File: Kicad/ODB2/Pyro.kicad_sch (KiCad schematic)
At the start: 33 parts, among them U11 TLV2372, U12 74LVC2G08GT_115, U13 TLV2372

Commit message: ajout footprints
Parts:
- Pyros_LED1, Pyros_LED2, Pyros_LED3: footprint (none) -> LED_SMD:LED_0805_2012Metric
- Pyros_R1, Pyros_R10, Pyros_R11, Pyros_R12, Pyros_R13, Pyros_R14, Pyros_R15, Pyros_R16, Pyros_R17, Pyros_R18, Pyros_R19, Pyros_R2, Pyros_R3, Pyros_R4, Pyros_R5, Pyros_R6, Pyros_R7, Pyros_R8, Pyros_R9: footprint (none) -> Resistor_SMD:R_0805_2012Metric
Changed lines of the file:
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@@
 			)
 		)
-		(property "Footprint" ""
+		(property "Footprint" "Resistor_SMD:R_0805_2012Metric"
 			(at 166.37 36.322 90)
 			(effects
@@
 			)
 		)
-		(property "Footprint" ""
+		(property "Footprint" "LED_SMD:LED_0805_2012Metric"
 			(at 95.25 176.53 0)
 			(effects
@@
 			)
 		)
-		(property "Footprint" ""
+		(property "Footprint" "Resistor_SMD:R_0805_2012Metric"
 			(at 151.13 97.282 90)
 			(effects
@@
 			)
 		)
-		(property "Footprint" ""
+		(property "Footprint" "Resistor_SMD:R_0805_2012Metric"
 			(at 41.91 96.012 90)
 			(effects
@@
 			)
 		)
-		(property "Footprint" ""
+		(property "Footprint" "Resistor_SMD:R_0805_2012Metric"
 			(at 56.388 72.39 90)
 			(effects
@@
 			)
 		)
-		(property "Footprint" ""
+		(property "Footprint" "Resistor_SMD:R_0805_2012Metric"
 			(at 71.882 82.55 90)
 			(effects
@@
 			)
 		)
-		(property "Footprint" ""
+		(property "Footprint" "Resistor_SMD:R_0805_2012Metric"
 			(at 173.228 43.18 90)
 			(effects
@@
 			)
 		)
-		(property "Footprint" ""
+		(property "Footprint" "Resistor_SMD:R_0805_2012Metric"
 			(at 50.038 104.14 90)
 			(effects
@@
 			)
 		)
-		(property "Footprint" ""
+		(property "Footprint" "Resistor_SMD:R_0805_2012Metric"
 			(at 181.102 83.82 90)
 			(effects
@@
 			)
 		)
-		(property "Footprint" ""
+		(property "Footprint" "Resistor_SMD:R_0805_2012Metric"
 			(at 168.148 109.22 90)
 			(effects
@@
 			)
 		)
-		(property "Footprint" ""
+		(property "Footprint" "Resistor_SMD:R_0805_2012Metric"
 			(at 58.928 107.95 90)
 			(effects
@@
 			)
 		)
-		(property "Footprint" ""
+		(property "Footprint" "Resistor_SMD:R_0805_2012Metric"
 			(at 165.608 73.66 90)
 			(effects
@@
 			)
 		)
-		(property "Footprint" ""
+		(property "Footprint" "Resistor_SMD:R_0805_2012Metric"
 			(at 57.15 35.052 90)
 			(effects
@@
 			)
 		)
-		(property "Footprint" ""
+		(property "Footprint" "Resistor_SMD:R_0805_2012Metric"
 			(at 41.91 174.752 90)
 			(effects
@@
 			)
 		)
-		(property "Footprint" ""
+		(property "Footprint" "LED_SMD:LED_0805_2012Metric"
 			(at 52.07 176.53 0)
 			(effects
@@
 			)
 		)
-		(property "Footprint" ""
+		(property "Footprint" "Resistor_SMD:R_0805_2012Metric"
 			(at 78.74 57.658 90)
 			(effects
@@
 			)
 		)
-		(property "Footprint" ""
+		(property "Footprint" "Resistor_SMD:R_0805_2012Metric"
 			(at 64.008 41.91 90)
 			(effects
@@
 			)
 		)
-		(property "Footprint" ""
+		(property "Footprint" "Resistor_SMD:R_0805_2012Metric"
 			(at 187.96 58.928 90)
 			(effects
@@
 			)
 		)
-		(property "Footprint" ""
+		(property "Footprint" "Resistor_SMD:R_0805_2012Metric"
 			(at 129.54 174.752 90)
 			(effects
@@
 			)
 		)
-		(property "Footprint" ""
+		(property "Footprint" "Resistor_SMD:R_0805_2012Metric"
 			(at 85.09 174.752 90)
 			(effects
@@
 			)
 		)
-		(property "Footprint" ""
+		(property "Footprint" "Resistor_SMD:R_0805_2012Metric"
 			(at 159.258 105.41 90)
 			(effects
@@
 			)
 		)
-		(property "Footprint" ""
+		(property "Footprint" "LED_SMD:LED_0805_2012Metric"
 			(at 139.7 176.53 0)
 			(effects

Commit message: revision logic
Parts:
- removed Pyros_LED3: Green, LED_SMD:LED_0805_2012Metric, symbol Device:LED
- removed Pyros_NPN3, Pyros_NPN4: MMBT3904, Package_TO_SOT_SMD:SOT-23, symbol Transistor_BJT:MMBT3904
- removed Pyros_R19: 68R ±1%, Resistor_SMD:R_0805_2012Metric, symbol Device:R
- removed U12: 74LVC2G08GT_115, Library:XSON8_SOT833-1_NEX, symbol ODB_Lib:74LVC2G08GT_115
- added Pyros_C1, Pyros_C2: 100nF, symbol Device:C
- added Pyros_PNP1, Pyros_PNP2: BC857, Package_TO_SOT_SMD:SOT-23, symbol Transistor_BJT:BC857
- added Pyros_XNOR: 74LV1T87GXH, 74LV1T87GXH:IC_74LV1T87GXH, symbol ODB_Lib:74LV1T87GXH
- added U12: SN74HC08DR, D14, symbol ODB_Lib:SN74HC08DR
- Pyros_R11: value 390R ±1% -> 1k5
- Pyros_R12: value 1k5 -> 390R ±1%
- Pyros_R15: value 1k5 -> 10k
- Pyros_R18: value 10k -> 68R ±1%
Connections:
- net +3V3: now also Pyros_R14.2, Pyros_R2.2, Pyros_C1.2, Pyros_C2.1, Pyros_PNP1.2 (E), Pyros_PNP2.2 (E), Pyros_XNOR.5 (VCC), U12.14 (VCC)
- net +6V0: now also Pyros_R18.2
- net GND: now also Pyros_R15.2, Pyros_C1.1, Pyros_C2.2, Pyros_XNOR.3 (GND), U12.7 (GND); no longer Pyros_R14.1, Pyros_R18.2, Pyros_R2.1
- net Pyros_Bluetooth: now also U12.2 (1B); no longer Pyros_R15.2
- net Pyros_DrogueADC: now also Pyros_R12.2; no longer Pyros_R11.2
- net Pyros_DrogueODB: now also U12.9 (3A)
- net Pyros_DrogueOn: now also U12.8 (3Y)
- net Pyros_MainODB: now also U12.5 (2B)
- net Pyros_MainOn: now also U12.6 (2Y)
- net at Pyros_R12.1: now also Pyros_R15.1, U13.2 (-); no longer Pyros_R14.2
- net at Pyros_R10.2, Pyros_R9.1: now also Pyros_NPN1.1 (B)
- net at Pyros_MOSFET2.4 (G), Pyros_R13.2: now also Pyros_NPN1.2 (E)
- net at Pyros_R3.1: now also Pyros_PNP1.3 (C); no longer Pyros_NPN1.2 (E)
- net Pyros_Test renamed ~Pyros_Test
- net ~Pyros_Test: now also Pyros_R11.2, Pyros_XNOR.1 (B); no longer Pyros_R12.2
- new net: Pyros_PNP1.1 (B), Pyros_R1.1, Pyros_R2.1
- new net: Pyros_PNP2.3 (C), Pyros_R18.1
- new net: Pyros_PNP2.1 (B), Pyros_R11.1, Pyros_R14.1
- new net: Pyros_XNOR.2 (A), U12.3 (1Y)
- new net: Pyros_XNOR.4 (Y), U12.10 (3B), U12.4 (2A)
- new net 6vEnable: U12.1 (1A)
- no-connect marks 0 -> 3
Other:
- note added: "Feu = 6vEnable x Bluetooth Test = ~Pyros_Test"
- note added: "ODB = lequel faire sauter ou tester?"
- note added: "Test Main = ~Pyros_Test x MainODB Test Drogue = ~Pyros_Test x DrogueODB Feu Main = (6vEnable x Bluetooth) x MainODB Feu Drogue = (6vEnable x Bluetooth) x DrogueODB où (6vEnable x Bluetooth) = 1 != ~Pyros_Test = 1 -> XNOR"
- note added: "pull-up"
- note removed: "Fire = On x 6V0"
- note removed: "On = ODB x Bluetooth"
- moved on the sheet: Pyros_LED1, Pyros_LED2, Pyros_R1, Pyros_R16, Pyros_R17, U11C

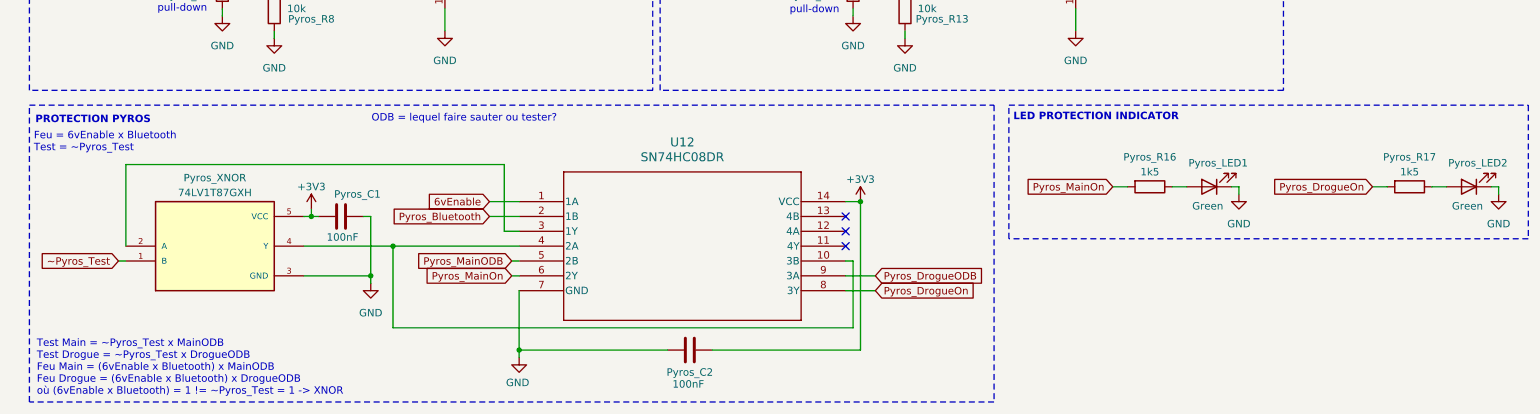
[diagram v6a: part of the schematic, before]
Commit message: ajout lecture tension batteries 1s / 2s
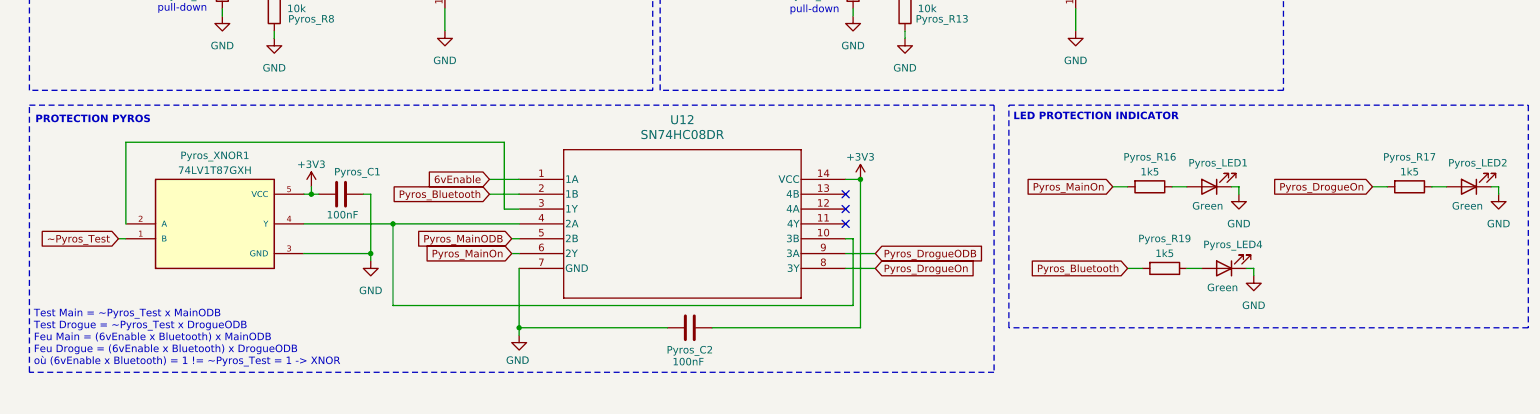
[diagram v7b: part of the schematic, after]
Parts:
- added Pyros_LED4: Green, LED_SMD:LED_0805_2012Metric, symbol Device:LED
- added Pyros_R19: 1k5, Resistor_SMD:R_0805_2012Metric, symbol Device:R
- Pyros_C1, Pyros_C2: footprint (none) -> Capacitor_SMD:C_0805_2012Metric
- renumbered Pyros_XNOR to Pyros_XNOR1
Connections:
- net GND: now also Pyros_LED4.1 (K)
- net Pyros_Bluetooth: now also Pyros_R19.2
- new net: Pyros_LED4.2 (A), Pyros_R19.1
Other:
- note removed: "Feu = 6vEnable x Bluetooth Test = ~Pyros_Test"
- note removed: "ODB = lequel faire sauter ou tester?"
- moved on the sheet: Pyros_C1, Pyros_C2, Pyros_XNOR1, U12

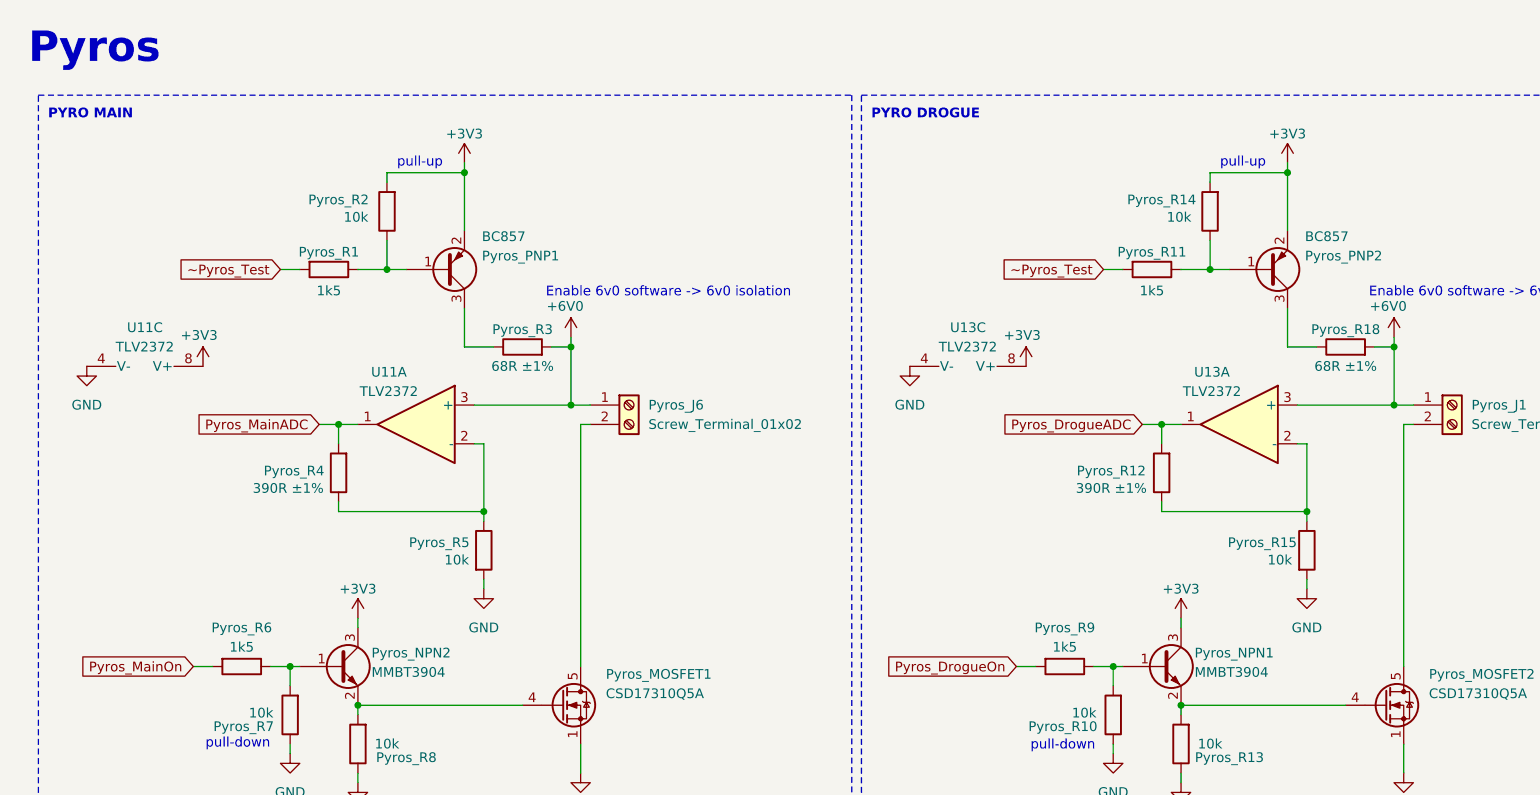
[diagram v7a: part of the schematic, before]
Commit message: WIP on ODB
buzzer résistance et footprints ampliop et autre
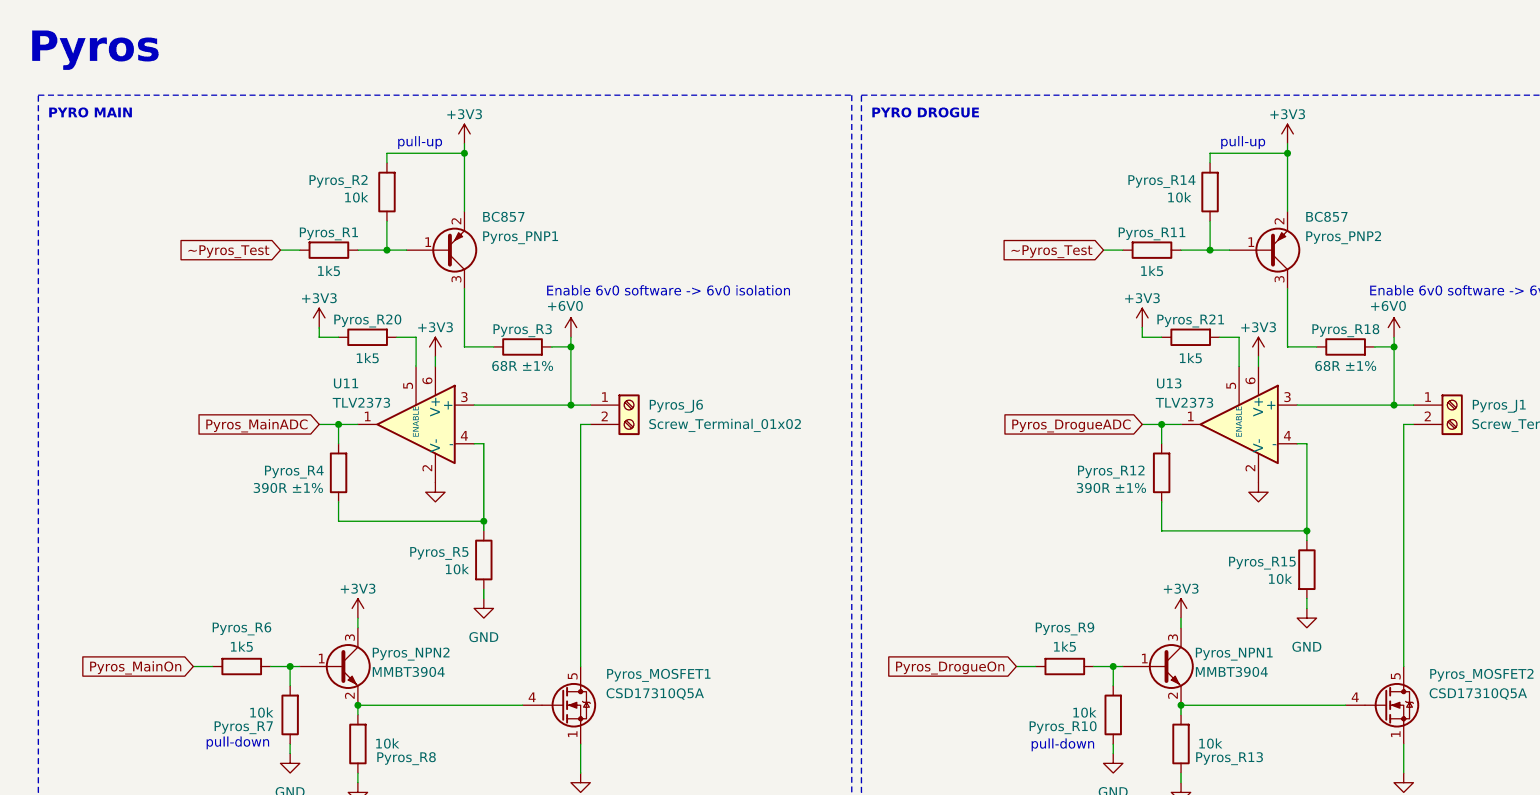
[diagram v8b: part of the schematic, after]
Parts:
- removed U11, U13: TLV2372, symbol Amplifier_Operational:TLV2372
- added Pyros_R20, Pyros_R21: 1k5, Resistor_SMD:R_0805_2012Metric, symbol Device:R
- added U11, U13: TLV2373, Package_TO_SOT_SMD:SOT-23-6, symbol Amplifier_Operational:OPA355NA
- U12: footprint D14 -> Package_SO:SOIC-14_3.9x8.7mm_P1.27mm
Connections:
- net +3V3: now also Pyros_R20.1, Pyros_R21.1, U11.6 (V+), U13.6 (V+)
- net +6V0: now also U11.3 (+), U13.3 (+)
- net GND: now also U11.2 (V-), U13.2 (V-)
- net Pyros_DrogueADC: now also U13.1
- net Pyros_MainADC: now also U11.1
- net at Pyros_R12.1, Pyros_R15.1: now also U13.4 (-)
- net at Pyros_R4.1, Pyros_R5.1: now also U11.4 (-)
- new net: Pyros_R20.2, U11.5 (ENABLE)
- new net: Pyros_R21.2, U13.5 (ENABLE)
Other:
- moved on the sheet: Pyros_PNP1, Pyros_PNP2, Pyros_R1, Pyros_R11, Pyros_R14, Pyros_R15, Pyros_R2, Pyros_R5
